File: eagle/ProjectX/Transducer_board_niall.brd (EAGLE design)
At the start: 100 x 100 mm, 104 parts, among them T1 MA40S4S, T10 MA40S4S, T100 MA40S4S, T11 MA40S4S, T12 MA40S4S, T13 MA40S4S, T14 MA40S4S, T15 MA40S4S, T16 MA40S4S, T17 MA40S4S, T18 MA40S4S, T19 MA40S4S, T2 MA40S4S, T20 MA40S4S, T21 MA40S4S, T22 MA40S4S, T23 MA40S4S, T24 MA40S4S, T25 MA40S4S, T26 MA40S4S, T27 MA40S4S, T28 MA40S4S, T29 MA40S4S, T3 MA40S4S, T30 MA40S4S, T31 MA40S4S, T32 MA40S4S, T33 MA40S4S, T34 MA40S4S, T35 MA40S4S, T36 MA40S4S, T37 MA40S4S, T38 MA40S4S, T39 MA40S4S, T4 MA40S4S, T40 MA40S4S, T41 MA40S4S, T42 MA40S4S, T43 MA40S4S, T44 MA40S4S, T45 MA40S4S, T46 MA40S4S, T47 MA40S4S, T48 MA40S4S, T49 MA40S4S, T5 MA40S4S, T50 MA40S4S, T51 MA40S4S, T52 MA40S4S, T53 MA40S4S, T54 MA40S4S, T55 MA40S4S, T56 MA40S4S, T57 MA40S4S, T58 MA40S4S, T59 MA40S4S, T6 MA40S4S, T60 MA40S4S, T61 MA40S4S, T62 MA40S4S, T63 MA40S4S, T64 MA40S4S, T65 MA40S4S, T66 MA40S4S, T67 MA40S4S, T68 MA40S4S, T69 MA40S4S, T7 MA40S4S, T70 MA40S4S, T71 MA40S4S, T72 MA40S4S, T73 MA40S4S, T74 MA40S4S, T75 MA40S4S, T76 MA40S4S, T77 MA40S4S, T78 MA40S4S, T79 MA40S4S, T8 MA40S4S, T80 MA40S4S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

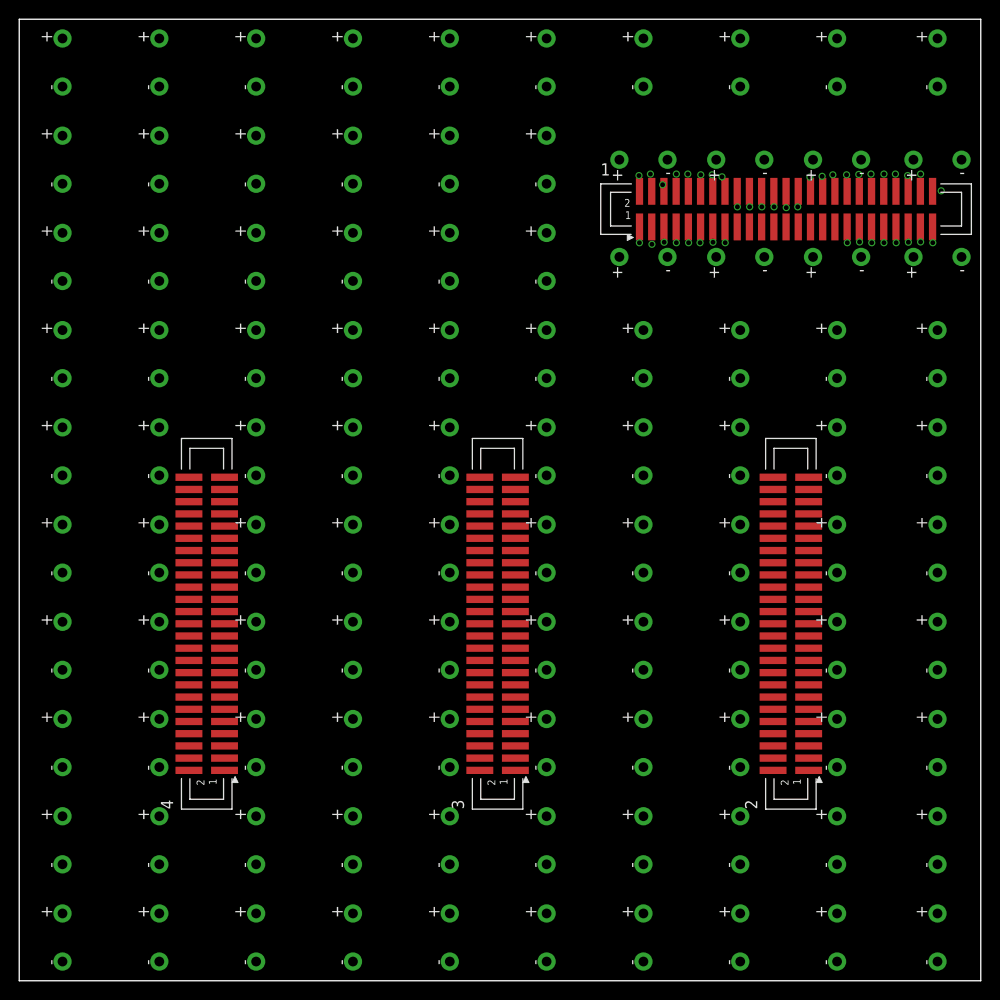
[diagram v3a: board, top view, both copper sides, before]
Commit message: Transievers routed
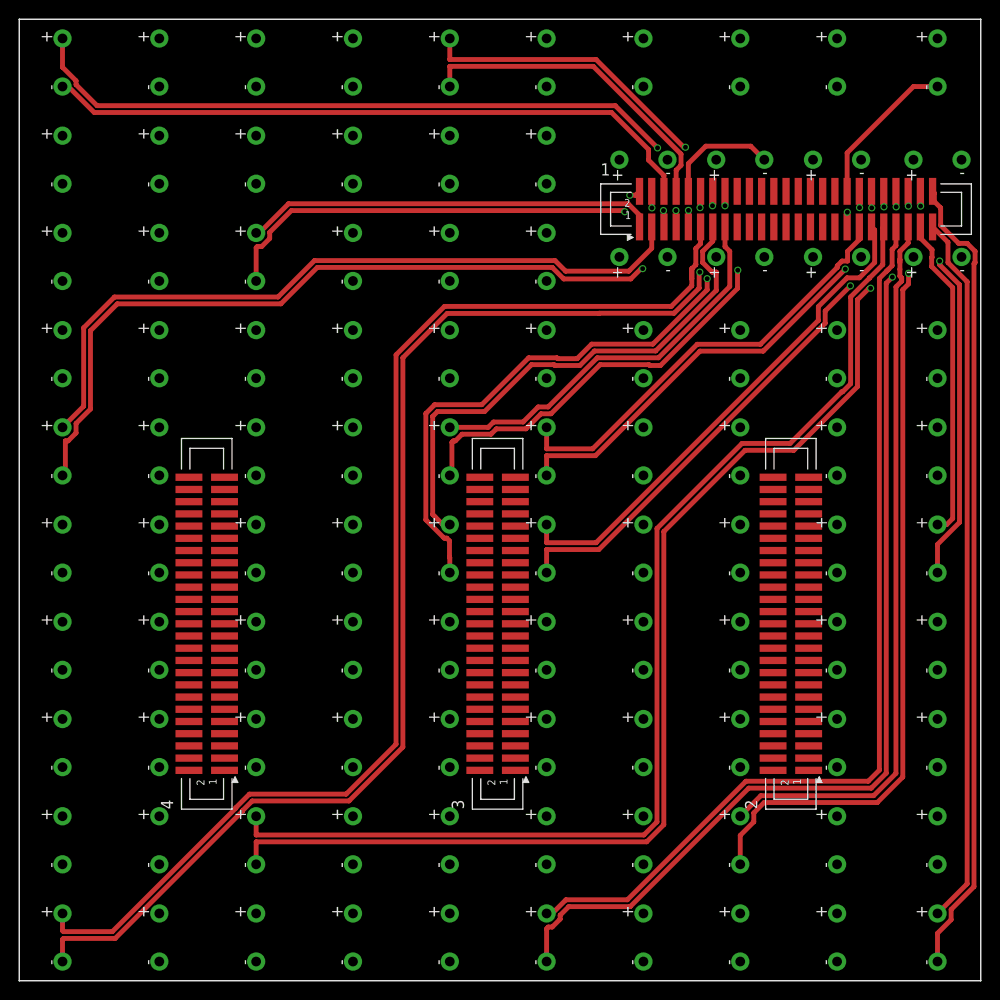
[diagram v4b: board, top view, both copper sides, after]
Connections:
- net FROM_T_1: now also 1.12; no longer 1.2
- net FROM_T_100: now also 1.50; no longer 1.48
- net FROM_T_22: now also 1.42; no longer 1.40
- net FROM_T_28: now also 1.2; no longer 1.12
- net FROM_T_55: now also 1.38; no longer 1.36
- net FROM_T_56: now also 1.40; no longer 1.38
- net FROM_T_60: now also 1.44; no longer 1.10
- net FROM_T_72: now also 1.10; no longer 1.42
- net FROM_T_79: now also 1.46; no longer 1.44
- net FROM_T_91: now also 1.36; no longer 1.50
- net FROM_T_96: now also 1.48; no longer 1.46
- net TO_T_1: now also 1.11; no longer 1.1
- net TO_T_100: now also 1.49; no longer 1.47
- net TO_T_22: now also 1.41; no longer 1.39
- net TO_T_28: now also 1.1; no longer 1.11
- net TO_T_55: now also 1.37; no longer 1.35
- net TO_T_56: now also 1.39; no longer 1.37
- net TO_T_60: now also 1.43; no longer 1.9
- net TO_T_72: now also 1.9; no longer 1.41
- net TO_T_79: now also 1.45; no longer 1.43
- net TO_T_91: now also 1.35; no longer 1.49
- net TO_T_96: now also 1.47; no longer 1.45
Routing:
- net FROM_T_1: track 0.00 -> 130.8 mm, vias 1 -> 2
- net TO_T_1: track 0.00 -> 126.5 mm, vias 1 -> 0
- net FROM_T_22: track 0.00 -> 123.9 mm, vias 1 -> 2
- net TO_T_22: track 0.00 -> 118.8 mm, vias 1 -> 0
- net FROM_T_60: track 0.00 -> 106.7 mm, vias 1 -> 2
- net TO_T_60: track 0.00 -> 98.3 mm, vias 1 -> 0
- net FROM_T_6: track 0.00 -> 86.0 mm, vias 1 -> 2
- net FROM_T_79: track 0.00 -> 85.4 mm, vias 1 -> 2
- net FROM_T_100: track 0.00 -> 84.1 mm, vias 1 -> 0
- net TO_T_10: track 0.00 -> 78.0 mm, vias 1 -> 2
- net TO_T_6: track 0.00 -> 76.9 mm, vias 1 -> 0
- net TO_T_79: track 0.00 -> 75.9 mm, vias 1 -> 0
- net TO_T_100: track 0.00 -> 74.2 mm, vias 1 -> 0
- net FROM_T_10: track 0.00 -> 68.7 mm, vias 1 -> 0
- net FROM_T_45: track 0.00 -> 63.7 mm, vias 1 -> 2
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
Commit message: More board work
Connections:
- net FROM_T_17: now also 4.17
- net FROM_T_18: now also 4.12
- net FROM_T_19: now also 4.5
- net FROM_T_2: now also 4.8
- net FROM_T_20: now also 4.4
- net FROM_T_21: now also 4.1
- net FROM_T_23: now also 4.9
- net FROM_T_24: now also 4.16
- net FROM_T_3: now also 4.13
- net FROM_T_4: now also 4.20
- net FROM_T_49: now also 1.18
- net FROM_T_51: now also 1.24
- net FROM_T_52: now also 1.20; no longer 1.22
- net FROM_T_53: no longer 1.24
- net FROM_T_68: no longer 1.20
- net FROM_T_69: now also 1.22; no longer 1.26
- net FROM_T_70: now also 1.26
- net FROM_T_71: now also 1.28
- net FROM_T_73: no longer 1.18
- net FROM_T_88: no longer 1.30
- net FROM_T_89: now also 1.32; no longer 1.28
- net FROM_T_90: now also 1.30
- net FROM_T_92: now also 1.34; no longer 1.32
- net FROM_T_93: no longer 1.34
- net TO_T_17: now also 4.18
- net TO_T_18: now also 4.11
- net TO_T_19: now also 4.6
- net TO_T_2: now also 4.7
- net TO_T_20: now also 4.3
- net TO_T_21: now also 4.2
- net TO_T_23: now also 4.10
- net TO_T_24: now also 4.15
- net TO_T_3: now also 4.14
- net TO_T_4: now also 4.19
- net TO_T_49: now also 1.17
- net TO_T_51: now also 1.23
- net TO_T_52: now also 1.19; no longer 1.21
- net TO_T_53: no longer 1.23
- net TO_T_68: no longer 1.19
- net TO_T_69: now also 1.21; no longer 1.25
- net TO_T_70: now also 1.25
- net TO_T_71: now also 1.27
- net TO_T_73: no longer 1.17
- net TO_T_88: no longer 1.29
- net TO_T_89: now also 1.31; no longer 1.27
- net TO_T_90: now also 1.29
- net TO_T_92: now also 1.33; no longer 1.31
- net TO_T_93: no longer 1.33
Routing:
- net TO_T_51: track 0.00 -> 39.3 mm, vias 0 -> 1
- net TO_T_49: track 0.00 -> 38.3 mm, vias 0 -> 1
- net FROM_T_51: track 0.00 -> 34.8 mm, vias 0 -> 1
- net FROM_T_49: track 0.00 -> 31.5 mm, vias 0 -> 1
- net TO_T_70: track 0.00 -> 30.2 mm, vias 0 -> 1
- net TO_T_52: track 0.00 -> 28.9 mm, vias 0 -> 1
- net TO_T_2: track 0.00 -> 25.4 mm, vias 0 -> 1
- net FROM_T_20: track 0.00 -> 24.4 mm, vias 0 -> 1
- net FROM_T_52: track 0.00 -> 24.0 mm, vias 0 -> 1
- net TO_T_69: track 0.00 -> 23.7 mm, vias 0 -> 1
- net TO_T_71: track 0.00 -> 22.6 mm, vias 0 -> 1
- net FROM_T_70: track 0.00 -> 22.6 mm, vias 0 -> 1
- net FROM_T_3: track 0.00 -> 22.2 mm, vias 0 -> 1
- net TO_T_90: track 0.00 -> 21.7 mm, vias 0 -> 1
- net TO_T_20: track 0.00 -> 21.6 mm, vias 0 -> 1
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
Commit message: Tangled web
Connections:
- net FROM_T_11: now also 4.49
- net FROM_T_12: now also 4.44
- net FROM_T_13: now also 4.37
- net FROM_T_14: now also 4.33
- net FROM_T_15: now also 4.28
- net FROM_T_16: now also 4.24
- net FROM_T_25: now also 4.21
- net FROM_T_26: now also 4.41
- net FROM_T_27: now also 4.32
- net FROM_T_29: now also 4.29
- net FROM_T_30: now also 4.48
- net FROM_T_5: now also 4.25
- net FROM_T_7: now also 4.36
- net FROM_T_8: now also 4.40
- net FROM_T_9: now also 4.45
- net TO_T_11: now also 4.50
- net TO_T_12: now also 4.43
- net TO_T_13: now also 4.38
- net TO_T_14: now also 4.34
- net TO_T_15: now also 4.27
- net TO_T_16: now also 4.23
- net TO_T_25: now also 4.22
- net TO_T_26: now also 4.42
- net TO_T_27: now also 4.31
- net TO_T_29: now also 4.30
- net TO_T_30: now also 4.47
- net TO_T_5: now also 4.26
- net TO_T_7: now also 4.35
- net TO_T_8: now also 4.39
- net TO_T_9: now also 4.46
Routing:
- net FROM_T_9: track 0.00 -> 67.5 mm, vias 0 -> 1
- net TO_T_29: track 0.00 -> 60.6 mm, vias 0 -> 3
- net TO_T_9: track 0.00 -> 59.8 mm, vias 0 -> 1
- net FROM_T_8: track 0.00 -> 53.5 mm, vias 0 -> 1
- net TO_T_11: track 0.00 -> 52.8 mm, vias 0 -> 1
- net FROM_T_29: track 0.00 -> 52.1 mm, vias 0 -> 1
- net TO_T_8: track 0.00 -> 50.8 mm, vias 0 -> 1
- net FROM_T_11: track 0.00 -> 50.6 mm, vias 0 -> 1
- net FROM_T_30: track 0.00 -> 48.9 mm, vias 0 -> 1
- net TO_T_30: track 0.00 -> 48.6 mm, vias 0 -> 1
- net TO_T_12: track 0.00 -> 45.5 mm, vias 0 -> 1
- net FROM_T_12: track 0.00 -> 40.1 mm, vias 0 -> 1
- net TO_T_13: track 0.00 -> 38.0 mm, vias 0 -> 1
- net TO_T_7: track 0.00 -> 37.6 mm, vias 0 -> 3
- net FROM_T_13: track 0.00 -> 35.9 mm, vias 0 -> 1
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
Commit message: Niall board better wiring
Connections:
- net FROM_T_12: now also 4.48; no longer 4.44
- net FROM_T_13: now also 4.44; no longer 4.37
- net FROM_T_14: now also 4.40; no longer 4.33
- net FROM_T_15: now also 4.36; no longer 4.28
- net FROM_T_16: now also 4.32; no longer 4.24
- net FROM_T_17: now also 4.28; no longer 4.17
- net FROM_T_18: now also 4.24; no longer 4.12
- net FROM_T_2: now also 4.9; no longer 4.8
- net FROM_T_20: now also 4.13; no longer 4.4
- net FROM_T_21: now also 4.17; no longer 4.1
- net FROM_T_23: now also 4.21; no longer 4.9
- net FROM_T_24: now also 4.25; no longer 4.16
- net FROM_T_25: now also 4.45; no longer 4.21
- net FROM_T_27: now also 4.37; no longer 4.32
- net FROM_T_29: now also 4.33; no longer 4.29
- net FROM_T_3: now also 4.1; no longer 4.13
- net FROM_T_30: now also 4.29; no longer 4.48
- net FROM_T_4: now also 4.4; no longer 4.20
- net FROM_T_5: now also 4.8; no longer 4.25
- net FROM_T_7: now also 4.12; no longer 4.36
- net FROM_T_8: now also 4.16; no longer 4.40
- net FROM_T_9: now also 4.20; no longer 4.45
- net TO_T_12: now also 4.46; no longer 4.43
- net TO_T_13: now also 4.42; no longer 4.38
- net TO_T_14: now also 4.38; no longer 4.34
- net TO_T_15: now also 4.34; no longer 4.27
- net TO_T_16: now also 4.30; no longer 4.23
- net TO_T_17: now also 4.26; no longer 4.18
- net TO_T_18: now also 4.22; no longer 4.11
- net TO_T_19: now also 4.7; no longer 4.6
- net TO_T_2: now also 4.11; no longer 4.7
- net TO_T_20: now also 4.15; no longer 4.3
- net TO_T_21: now also 4.19; no longer 4.2
- net TO_T_23: now also 4.23; no longer 4.10
- net TO_T_24: now also 4.27; no longer 4.15
- net TO_T_25: now also 4.47; no longer 4.22
- net TO_T_26: now also 4.43; no longer 4.42
- net TO_T_27: now also 4.39; no longer 4.31
- net TO_T_29: now also 4.35; no longer 4.30
- net TO_T_3: now also 4.3; no longer 4.14
- net TO_T_30: now also 4.31; no longer 4.47
- net TO_T_4: now also 4.2; no longer 4.19
- net TO_T_5: now also 4.6; no longer 4.26
- net TO_T_7: now also 4.10; no longer 4.35
- net TO_T_8: now also 4.14; no longer 4.39
- net TO_T_9: now also 4.18; no longer 4.46
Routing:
- net FROM_T_9: track 67.5 -> 143.8 mm
- net TO_T_51: track 39.3 -> 1.05 mm, vias 1 -> 0
- net TO_T_49: track 38.3 -> 1.73 mm, vias 1 -> 0
- net FROM_T_7: track 28.6 -> 64.7 mm
- net FROM_T_51: track 34.8 -> 1.89 mm, vias 1 -> 0
- net FROM_T_49: track 31.5 -> 0.00 mm, vias 1 -> 0
- net TO_T_7: track 37.6 -> 67.4 mm, vias 3 -> 1
- net TO_T_70: track 30.2 -> 1.74 mm, vias 1 -> 0
- net TO_T_9: track 59.8 -> 87.5 mm
- net TO_T_52: track 28.9 -> 1.75 mm, vias 1 -> 0
- net TO_T_8: track 50.8 -> 77.7 mm
- net TO_T_5: track 19.1 -> 45.0 mm, vias 2 -> 1
- net TO_T_30: track 48.6 -> 74.3 mm
- net FROM_T_27: track 34.1 -> 57.6 mm, vias 3 -> 1
- net FROM_T_5: track 19.5 -> 42.9 mm, vias 2 -> 1
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
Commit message: Fixed top right section of board
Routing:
- net TO_T_51: track 1.05 -> 45.2 mm, vias 0 -> 1
- net TO_T_49: track 1.73 -> 42.3 mm, vias 0 -> 1
- net TO_T_89: track 1.74 -> 42.1 mm, vias 0 -> 1
- net FROM_T_49: track 0.00 -> 38.8 mm, vias 0 -> 1
- net FROM_T_89: track 2.94 -> 37.9 mm, vias 0 -> 1
- net FROM_T_51: track 1.89 -> 33.6 mm, vias 0 -> 1
- net FROM_T_52: track 2.89 -> 33.6 mm, vias 0 -> 1
- net TO_T_52: track 1.75 -> 30.0 mm, vias 0 -> 1
- net TO_T_70: track 1.74 -> 28.3 mm, vias 0 -> 1
- net TO_T_71: track 1.71 -> 26.5 mm, vias 0 -> 1
- net FROM_T_70: track 1.59 -> 26.1 mm, vias 0 -> 1
- net TO_T_69: track 1.75 -> 23.3 mm, vias 0 -> 1
- net TO_T_90: track 1.70 -> 22.2 mm, vias 0 -> 1
- net TO_T_92: track 1.61 -> 21.9 mm, vias 0 -> 1
- net FROM_T_92: track 1.87 -> 20.6 mm, vias 0 -> 1
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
